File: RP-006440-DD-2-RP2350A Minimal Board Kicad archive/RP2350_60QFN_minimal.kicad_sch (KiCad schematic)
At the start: 45 parts, among them J1 USB_C_Receptacle_USB2.0_16P, J2 Conn_02x18_Odd_Even, J3 Conn_02x18_Odd_Even, J4 SM03B-SRSS-TB, SW1 SW_Push, SW2 SW_Push, U1 RP2350_60QFN, U2 NCP1117-3.3_SOT223, U3 W25Q128JVS, Y1 ABM8-272-T3

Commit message: Update PCB
added usbc receptacle and resistor footprints to pcb
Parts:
- R11, R3: footprint (none) -> Resistor_SMD:R_0402_1005Metric
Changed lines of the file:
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@@
 			)
 		)
-		(property "Footprint" ""
+		(property "Footprint" "Resistor_SMD:R_0402_1005Metric"
 			(at 67.31 39.878 90)
 			(effects
@@
 			)
 		)
-		(property "Footprint" ""
+		(property "Footprint" "Resistor_SMD:R_0402_1005Metric"
 			(at 74.93 36.068 90)
 			(effects

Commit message: Schematic text
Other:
- note added: "according to USB Type-C Specification Release 1.3. 5.1K ohm resistor to ground on CC1/2 for Sink Termination"
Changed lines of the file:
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@@
+		)
+	)
+	(text "according to USB Type-C Specification Release 1.3.\n5.1K ohm resistor to ground on CC1/2 for Sink Termination"
+		(exclude_from_sim no)
+		(at 96.52 55.372 0)
+		(effects
+			(font
+				(size 1.27 1.27)
+			)
 		)
 	)

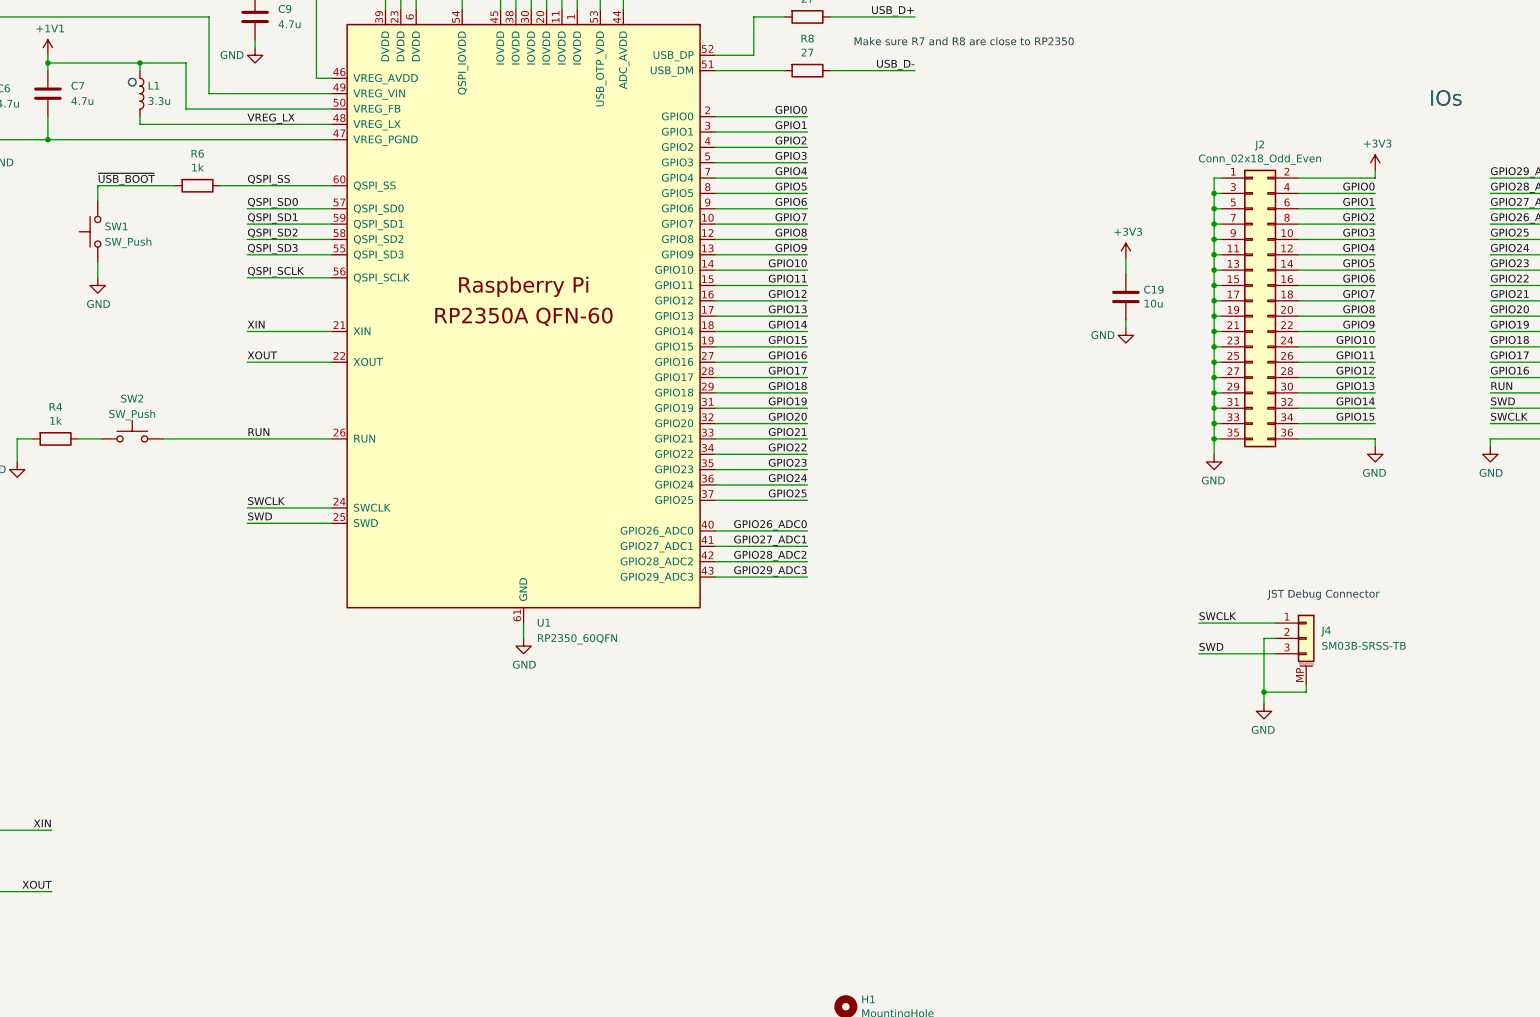
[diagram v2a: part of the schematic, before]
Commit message: Added debugprobe schematic
Added debugprobe schematic and started working on debug probe circuit
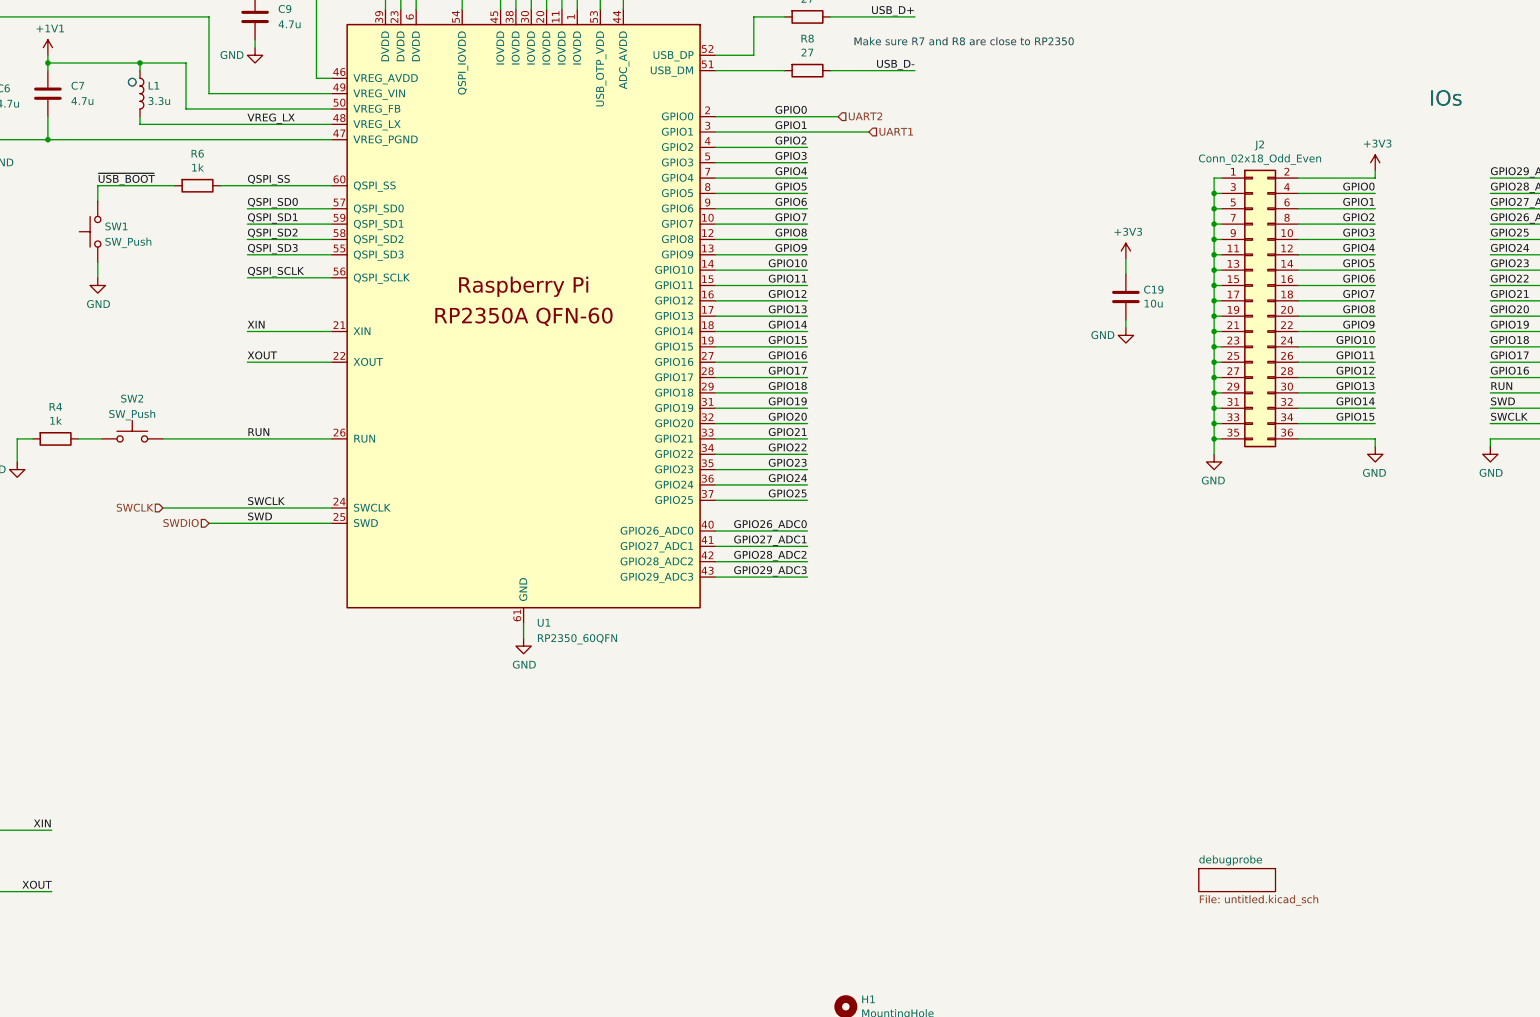
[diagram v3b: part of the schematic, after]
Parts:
- removed J4: SM03B-SRSS-TB, Connector_JST:JST_SH_SM03B-SRSS-TB_1x03-1MP_P1.00mm_Horizontal, symbol Connector_Generic_MountingPin:Conn_01x03_MountingPin
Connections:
- net GPIO0 renamed UART2
- net GPIO1 renamed UART1
- net SWD renamed SWDIO
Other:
- added sheet debugprobe (untitled.kicad_sch)
- note removed: "JST Debug Connector"
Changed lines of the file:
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@@
 	)
 	(junction
-		(at 320.675 207.01)
-		(diameter 0)
-		(color 0 0 0 0)
-	)
-	(junction
 		(at 257.81 60.96)
 		(diameter 0)
@@
 	(wire
 		(pts
-			(xy 320.675 198.12) (xy 320.675 207.01)
-		)
-		(stroke
-			(width 0)
-			(type default)
-		)
-	)
-	(wire
-		(pts
 			(xy 71.12 34.29) (xy 58.42 34.29)
 		)
@@
 	(wire
 		(pts
-			(xy 229.87 111.76) (xy 245.11 111.76)
+			(xy 229.87 111.76) (xy 250.19 111.76)
 		)
 		(stroke
@@
 	(wire
 		(pts
-			(xy 166.37 176.53) (xy 152.4 176.53)
+			(xy 166.37 176.53) (xy 138.43 176.53)
 		)
 		(stroke
@@
 	(wire
 		(pts
-			(xy 229.87 114.3) (xy 245.11 114.3)
+			(xy 229.87 114.3) (xy 255.27 114.3)
 		)
 		(stroke
@@
 	(wire
 		(pts
-			(xy 327.66 205.74) (xy 327.66 207.01)
-		)
-		(stroke
-			(width 0)
-			(type default)
-		)
-	)
-	(wire
-		(pts
 			(xy 370.84 160.02) (xy 358.14 160.02)
 		)
@@
 	(wire
 		(pts
-			(xy 309.88 200.66) (xy 322.58 200.66)
-		)
-		(stroke
-			(width 0)
-			(type default)
-		)
-	)
-	(wire
-		(pts
 			(xy 384.81 157.48) (xy 384.81 160.02)
 		)
@@
 	(wire
 		(pts
+			(xy 146.05 179.07) (xy 166.37 179.07)
+		)
+		(stroke
+			(width 0)
+			(type default)
+		)
+	)
+	(wire
+		(pts
 			(xy 269.24 62.23) (xy 269.24 60.96)
 		)
@@
 	(wire
 		(pts
-			(xy 166.37 179.07) (xy 152.4 179.07)
-		)
-		(stroke
-			(width 0)
-			(type default)
-		)
-	)
-	(wire
-		(pts
 			(xy 58.42 41.91) (xy 62.23 41.91)
 		)
@@
 	(wire
 		(pts
-			(xy 320.675 207.01) (xy 327.66 207.01)
-		)
-		(stroke
-			(width 0)
-			(type default)
-		)
-	)
-	(wire
-		(pts
 			(xy 384.81 162.56) (xy 384.81 165.1)
 		)
@@
 	(wire
 		(pts
-			(xy 309.88 195.58) (xy 322.58 195.58)
-		)
-		(stroke
-			(width 0)
-			(type default)
-		)
-	)
-	(wire
-		(pts
 			(xy 229.87 119.38) (xy 245.11 119.38)
 		)
@@
 	(wire
 		(pts
-			(xy 322.58 198.12) (xy 320.675 198.12)
-		)
-		(stroke
-			(width 0)
-			(type default)
-		)
-	)
-	(wire
-		(pts
 			(xy 88.265 229.87) (xy 120.015 229.87)
 		)
@@
 	(wire
 		(pts
-			(xy 320.675 207.01) (xy 320.675 208.915)
-		)
-		(stroke
-			(width 0)
-			(type default)
-		)
-	)
-	(wire
-		(pts
 			(xy 313.69 165.1) (xy 312.42 165.1)
 		)
@@
 		)
 	)
-	(text "JST Debug Connector"
-		(exclude_from_sim no)
-		(at 321.31 191.77 0)
-		(effects
-			(font
-				(size 1.27 1.27)
-			)
-			(justify left bottom)
-		)
-	)
 	(text "according to USB Type-C Specification Release 1.3.\n5.1K ohm resistor to ground on CC1/2 for Sink Termination"
 		(exclude_from_sim no)
@@
 		)
 	)
-	(label "SWCLK"
-		(at 309.88 195.58 0)
-		(effects
-			(font
-				(size 1.27 1.27)
-			)
-			(justify left bottom)
-		)
-	)
 	(label "QSPI_SD3"
 		(at 103.505 139.065 180)
@@
 		)
 	)
-	(label "SWD"
-		(at 309.88 200.66 0)
-		(effects
-			(font
-				(size 1.27 1.27)
-			)
-			(justify left bottom)
-		)
-	)
 	(label "GPIO14"
 		(at 339.09 160.02 180)
@@
 		)
 	)
+	(hierarchical_label "SWDIO"
+		(shape input)
+		(at 146.05 179.07 180)
+		(effects
+			(font
+				(size 1.27 1.27)
+			)
+			(justify right)
+		)
+	)
+	(hierarchical_label "UART1"
+		(shape input)
+		(at 255.27 114.3 0)
+		(effects
+			(font
+				(size 1.27 1.27)
+			)
+			(justify left)
+		)
+	)
+	(hierarchical_label "SWCLK"
+		(shape input)
+		(at 138.43 176.53 180)
+		(effects
+			(font
+				(size 1.27 1.27)
+			)
+			(justify right)
+		)
+	)
+	(hierarchical_label "UART2"
+		(shape input)
+		(at 250.19 111.76 0)
+		(effects
+			(font
+				(size 1.27 1.27)
+			)
+			(justify left)
+		)
+	)
 	(symbol
 		(lib_id "Memory_Flash:W25Q128JVS")
@@
 	(symbol
 		(lib_id "power:GND")
-		(at 320.675 208.915 0)
-		(mirror y)
-		(unit 1)
-		(exclude_from_sim no)
-		(in_bom yes)
-		(on_board yes)
-		(dnp no)
-		(property "Reference" "#PWR031"
-			(at 320.675 215.265 0)
-			(effects
-				(font
-					(size 1.27 1.27)
-				)
-				(hide yes)
-			)
-		)
-		(property "Value" "GND"
-			(at 320.548 213.3092 0)
-			(effects
-				(font
-					(size 1.27 1.27)
-				)
-			)
-		)
-		(property "Footprint" ""
-			(at 320.675 208.915 0)
-			(effects
-				(font
-					(size 1.27 1.27)
-				)
-				(hide yes)
-			)
-		)
-		(property "Datasheet" ""
-			(at 320.675 208.915 0)
-			(effects
-				(font
-					(size 1.27 1.27)
-				)
-				(hide yes)
-			)
-		)
-		(property "Description" ""
-			(at 320.675 208.915 0)
-			(effects
-				(font
-					(size 1.27 1.27)
-				)
-				(hide yes)
-			)
-		)
-		(pin "1"
-		)
-		(instances
-			(project "RP2350_60QFN_minimal"
-				(path "/94683f5c-9cd9-448e-be96-9792537b5cb8"
-					(reference "#PWR031")
-					(unit 1)
-				)
-			)
-		)
-	)
-	(symbol
-		(lib_id "power:GND")
 		(at 143.51 73.66 0)
 		(unit 1)
@@
 	)
 	(symbol
-		(lib_id "Connector_Generic_MountingPin:Conn_01x03_MountingPin")
-		(at 327.66 198.12 0)
-		(unit 1)
-		(exclude_from_sim no)
-		(in_bom yes)
-		(on_board yes)
-		(dnp no)
-		(fields_autoplaced yes)
-		(property "Reference" "J4"
-			(at 330.2 196.85 0)
-			(effects
-				(font
-					(size 1.27 1.27)
-				)
-				(justify left)
-			)
-		)
-		(property "Value" "SM03B-SRSS-TB"
-			(at 330.2 199.39 0)
-			(effects
-				(font
-					(size 1.27 1.27)
-				)
-				(justify left)
-			)
-		)
-		(property "Footprint" "Connector_JST:JST_SH_SM03B-SRSS-TB_1x03-1MP_P1.00mm_Horizontal"
-			(at 327.66 198.12 0)
-			(effects
-				(font
-					(size 1.27 1.27)
-				)
-				(hide yes)
-			)
-		)
-		(property "Datasheet" "~"
-			(at 327.66 198.12 0)
-			(effects
-				(font
-					(size 1.27 1.27)
-				)
-				(hide yes)
-			)
-		)
-		(property "Description" ""
-			(at 327.66 198.12 0)
-			(effects
-				(font
-					(size 1.27 1.27)
-				)
-				(hide yes)
-			)
-		)
-		(pin "1"
-		)
-		(pin "2"
-		)
-		(pin "3"
-		)
-		(pin "MP"
-		)
-		(instances
-			(project "RP2350_60QFN_minimal"
-				(path "/94683f5c-9cd9-448e-be96-9792537b5cb8"
-					(reference "J4")
-					(unit 1)
-				)
-			)
-		)
-	)
-	(symbol
 		(lib_name "GND_1")
 		(lib_id "power:GND")
@@
 				)
 			)
+		)
+	)
+	(sheet
+		(at 309.88 236.22)
+		(size 12.7 3.81)
+		(fields_autoplaced yes)
+		(stroke
+			(width 0.1524)
+			(type solid)
+		)
+		(fill
+			(color 0 0 0 0.0000)
+		)
+		(property "Sheetname" "debugprobe"
+			(at 309.88 235.5084 0)
+			(effects
+				(font
+					(size 1.27 1.27)
+				)
+				(justify left bottom)
+			)
+		)
+		(property "Sheetfile" "untitled.kicad_sch"
+			(at 309.88 240.6146 0)
+			(effects
+				(font
+					(size 1.27 1.27)
+				)
+				(justify left top)
+			)
+		)
+		(instances
+			(project "RP2350_60QFN_minimal"
+				(path "/94683f5c-9cd9-448e-be96-9792537b5cb8"
+					(page "2")
+				)
+			)

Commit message: small change
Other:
- moved on the sheet: C19
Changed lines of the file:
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@@
 	)
 	(junction
-		(at 88.9 38.1)
+		(at 82.55 38.1)
 		(diameter 0)
 		(color 0 0 0 0)
@@
 	(wire
 		(pts
-			(xy 88.9 38.1) (xy 88.9 39.37)
+			(xy 82.55 38.1) (xy 82.55 39.37)
 		)
 		(stroke
@@
 	(wire
 		(pts
-			(xy 78.74 34.29) (xy 88.9 34.29)
+			(xy 78.74 34.29) (xy 82.55 34.29)
 		)
 		(stroke
@@
 	(wire
 		(pts
-			(xy 88.9 34.29) (xy 88.9 38.1)
+			(xy 82.55 34.29) (xy 82.55 38.1)
 		)
 		(stroke
@@
 	(wire
 		(pts
-			(xy 71.12 38.1) (xy 88.9 38.1)
+			(xy 71.12 38.1) (xy 82.55 38.1)
 		)
 		(stroke
@@
 	(wire
 		(pts
-			(xy 297.815 135.255) (xy 297.815 137.795)
+			(xy 279.4 146.05) (xy 279.4 148.59)
 		)
 		(stroke
@@
 	(wire
 		(pts
-			(xy 297.815 145.415) (xy 297.815 146.685)
+			(xy 279.4 156.21) (xy 279.4 157.48)
 		)
 		(stroke
@@
 	(symbol
 		(lib_id "power:+3V3")
-		(at 297.815 135.255 0)
+		(at 279.4 146.05 0)
 		(unit 1)
 		(exclude_from_sim no)
@@
 		(dnp no)
 		(property "Reference" "#PWR027"
-			(at 297.815 139.065 0)
+			(at 279.4 149.86 0)
 			(effects
 				(font
@@
 		)
 		(property "Value" "+3V3"
-			(at 298.196 130.8608 0)
+			(at 279.781 141.6558 0)
 			(effects
 				(font
@@
 		)
 		(property "Footprint" ""
-			(at 297.815 135.255 0)
+			(at 279.4 146.05 0)
 			(effects
 				(font
@@
 		)
 		(property "Datasheet" ""
-			(at 297.815 135.255 0)
+			(at 279.4 146.05 0)
 			(effects
 				(font
@@
 		)
 		(property "Description" ""
-			(at 297.815 135.255 0)
+			(at 279.4 146.05 0)
 			(effects
 				(font
@@
 	(symbol
 		(lib_id "Device:C")
-		(at 297.815 141.605 0)
+		(at 279.4 152.4 0)
 		(unit 1)
 		(exclude_from_sim no)
@@
 		(dnp no)
 		(property "Reference" "C19"
-			(at 300.736 140.4366 0)
+			(at 282.321 151.2316 0)
 			(effects
 				(font
@@
 		)
 		(property "Value" "10u"
-			(at 300.736 142.748 0)
+			(at 282.321 153.543 0)
 			(effects
 				(font
@@
 		)
 		(property "Footprint" "Capacitor_SMD:C_0805_2012Metric"
-			(at 298.7802 145.415 0)
+			(at 280.3652 156.21 0)
 			(effects
 				(font
@@
 		)
 		(property "Datasheet" "~"
-			(at 297.815 141.605 0)
+			(at 279.4 152.4 0)
 			(effects
 				(font
@@
 		)
 		(property "Description" ""
-			(at 297.815 141.605 0)
+			(at 279.4 152.4 0)
 			(effects
 				(font
@@
 	(symbol
 		(lib_id "power:GND")
-		(at 297.815 146.685 0)
+		(at 279.4 157.48 0)
 		(unit 1)
 		(exclude_from_sim no)
@@
 		(dnp no)
 		(property "Reference" "#PWR028"
-			(at 297.815 153.035 0)
+			(at 279.4 163.83 0)
 			(effects
 				(font
@@
 		)
 		(property "Value" "GND"
-			(at 294.005 147.955 0)
+			(at 275.59 158.75 0)
 			(effects
 				(font
@@
 		)
 		(property "Footprint" ""
-			(at 297.815 146.685 0)
+			(at 279.4 157.48 0)
 			(effects
 				(font
@@
 		)
 		(property "Datasheet" ""
-			(at 297.815 146.685 0)
+			(at 279.4 157.48 0)
 			(effects
 				(font
@@
 		)
 		(property "Description" ""
-			(at 297.815 146.685 0)
+			(at 279.4 157.48 0)
 			(effects
 				(font
@@
 		(lib_name "GND_1")
 		(lib_id "power:GND")
-		(at 88.9 39.37 0)
+		(at 82.55 39.37 0)
 		(unit 1)
 		(exclude_from_sim no)
@@
 		(fields_autoplaced yes)
 		(property "Reference" "#PWR032"
-			(at 88.9 45.72 0)
+			(at 82.55 45.72 0)
 			(effects
 				(font
@@
 		)
 		(property "Value" "GND"
-			(at 88.9 44.45 0)
+			(at 82.55 44.45 0)
 			(effects
 				(font
@@
 		)
 		(property "Footprint" ""
-			(at 88.9 39.37 0)
+			(at 82.55 39.37 0)
 			(effects
 				(font
@@
 		)
 		(property "Datasheet" ""
-			(at 88.9 39.37 0)
+			(at 82.55 39.37 0)
 			(effects
 				(font
@@
 		)
 		(property "Description" "Power symbol creates a global label with name \"GND\" , ground"
-			(at 88.9 39.37 0)
+			(at 82.55 39.37 0)
 			(effects
 				(font
